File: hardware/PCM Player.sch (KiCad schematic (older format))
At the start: 0 parts

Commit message: Updated PCB
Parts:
- added H1, H2, H3, H4: MountingHole, MountingHole:MountingHole_3.2mm_M3, symbol Mechanical:MountingHole
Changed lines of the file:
@@
 F1 "PSU.sch" 50
 $EndSheet
+$Comp
+L Mechanical:MountingHole H2
+U 1 1 5ECA4AC5
+P 3950 1100
+F 0 "H2" H 4050 1146 50  0000 L CNN
+F 1 "MountingHole" H 4050 1055 50  0000 L CNN
+F 2 "MountingHole:MountingHole_3.2mm_M3" H 3950 1100 50  0001 C CNN
+F 3 "~" H 3950 1100 50  0001 C CNN
+	1    3950 1100
+	1    0    0    -1
+$EndComp
+$Comp
+L Mechanical:MountingHole H3
+U 1 1 5ECA4CB6
+P 4750 850
+F 0 "H3" H 4850 896 50  0000 L CNN
+F 1 "MountingHole" H 4850 805 50  0000 L CNN
+F 2 "MountingHole:MountingHole_3.2mm_M3" H 4750 850 50  0001 C CNN
+F 3 "~" H 4750 850 50  0001 C CNN
+	1    4750 850
+	1    0    0    -1
+$EndComp
+$Comp
+L Mechanical:MountingHole H4
+U 1 1 5ECA51A2
+P 4750 1100
+F 0 "H4" H 4850 1146 50  0000 L CNN
+F 1 "MountingHole" H 4850 1055 50  0000 L CNN
+F 2 "MountingHole:MountingHole_3.2mm_M3" H 4750 1100 50  0001 C CNN
+F 3 "~" H 4750 1100 50  0001 C CNN
+	1    4750 1100
+	1    0    0    -1
+$EndComp
+$Comp
+L Mechanical:MountingHole H1
+U 1 1 5ECA4559
+P 3950 850
+F 0 "H1" H 4050 896 50  0000 L CNN
+F 1 "MountingHole" H 4050 805 50  0000 L CNN
+F 2 "MountingHole:MountingHole_3.2mm_M3" H 3950 850 50  0001 C CNN
+F 3 "~" H 3950 850 50  0001 C CNN
+	1    3950 850
+	1    0    0    -1
+$EndComp
 $EndSCHEMATC

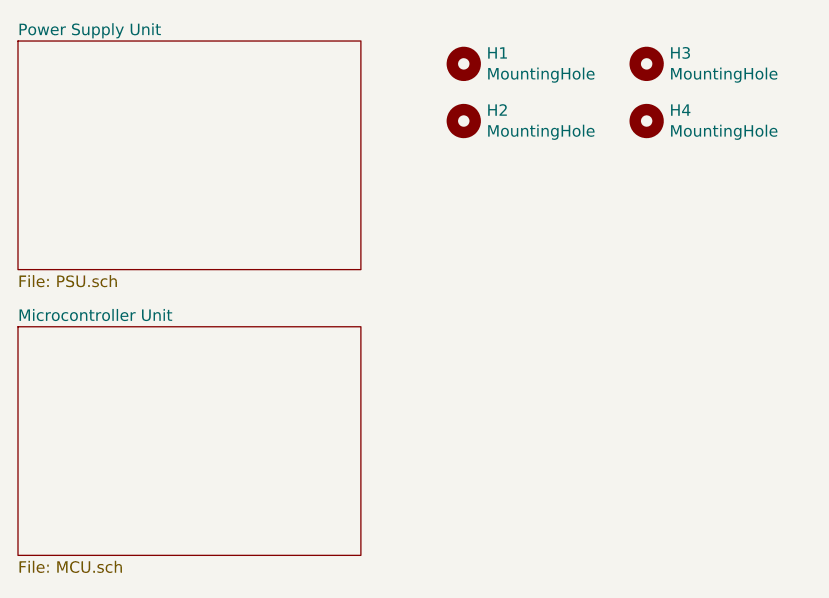
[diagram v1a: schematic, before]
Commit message: Added amplifier schematic
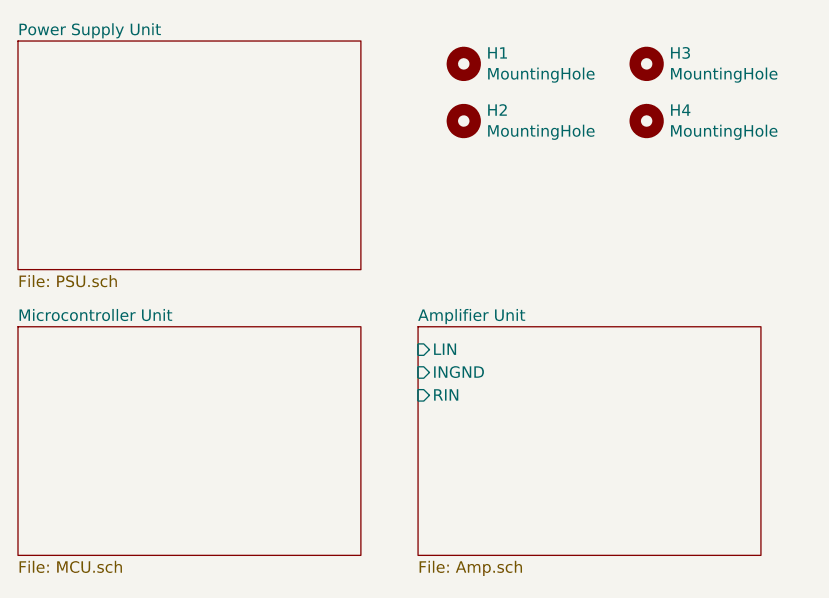
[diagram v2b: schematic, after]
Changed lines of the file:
@@
 EESchema Schematic File Version 4
-LIBS:PCM Player-cache
-EELAYER 29 0
+EELAYER 30 0
 EELAYER END
 $Descr A4 11693 8268
 encoding utf-8
-Sheet 1 3
+Sheet 1 4
 Title "PCM Player"
 Date "2020-05-07"
@@
 F0 "Microcontroller Unit" 50
 F1 "MCU.sch" 50
-$EndSheet
-$Sheet
-S 2000 750  1500 1000
-U 5EC8138E
-F0 "Power Supply Unit" 50
-F1 "PSU.sch" 50
 $EndSheet
 $Comp
@@
 	1    0    0    -1
 $EndComp
+$Sheet
+S 3750 2000 1500 1000
+U 5F12834A
+F0 "Amplifier Unit" 50
+F1 "Amp.sch" 50
+F2 "LIN" I L 3750 2100 50
+F3 "RIN" I L 3750 2300 50
+F4 "INGND" I L 3750 2200 50
+$EndSheet
+$Sheet
+S 2000 750  1500 1000
+U 5EC8138E
+F0 "Power Supply Unit" 50
+F1 "PSU.sch" 50
+$EndSheet
 $EndSCHEMATC
